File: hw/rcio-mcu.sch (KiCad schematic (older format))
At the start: 28 parts

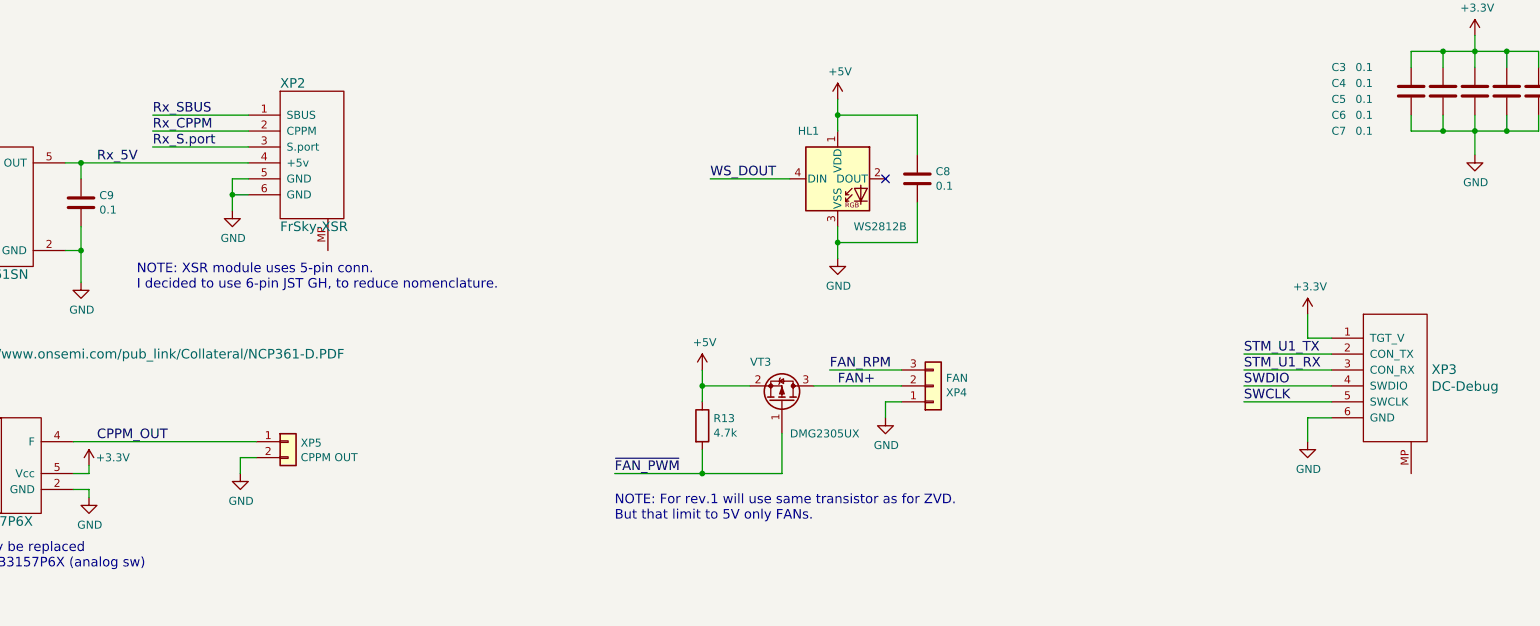
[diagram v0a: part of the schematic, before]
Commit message: hw: connect GH mount points with GND, add 3V battery
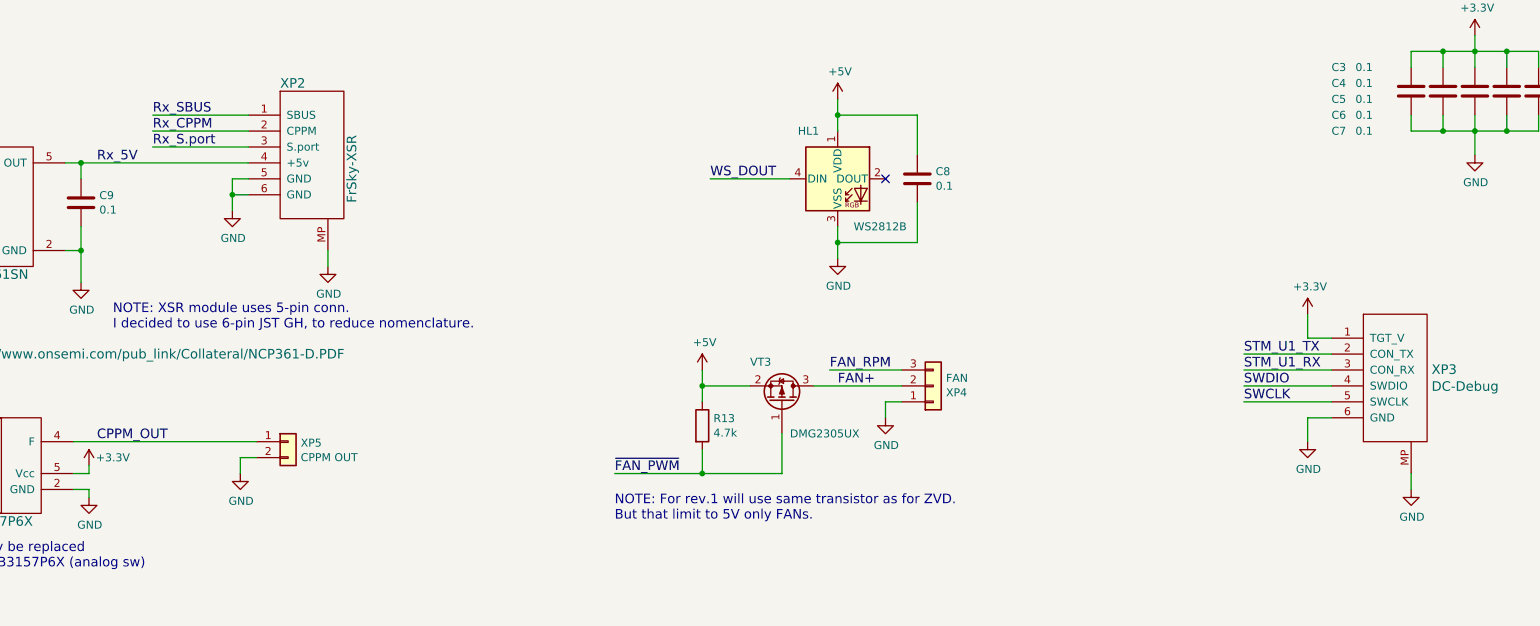
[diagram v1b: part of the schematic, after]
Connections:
- net GND: now also XP2.MP, XP3.MP
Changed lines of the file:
@@
 P 5650 6950
 F 0 "XP2" H 5450 7400 60  0000 L CNN
-F 1 "FrSky-XSR" H 5450 6500 60  0000 L CNN
+F 1 "FrSky-XSR" V 5900 6650 60  0000 L CNN
 F 2 "Connector_JST:JST_GH_SM06B-GHS-TB_1x06-1MP_P1.25mm_Horizontal" H 5650 6950 60  0001 C CNN
 F 3 "" H 5650 6950 60  0001 C CNN
@@
 	1    0    0    -1
 $EndComp
-Text Notes 4550 7800 0    60   ~ 0
+Text Notes 4400 8050 0    60   ~ 0
 NOTE: XSR module uses 5-pin conn.\nI decided to use 6-pin JST GH, to reduce nomenclature.
 $Comp
@@
 Wire Wire Line
 	10600 3250 13550 3250
+$Comp
+L power:GND #PWR?
+U 1 1 5ACFE321
+P 12550 9050
+F 0 "#PWR?" H 12550 8800 50  0001 C CNN
+F 1 "GND" H 12555 8877 50  0000 C CNN
+F 2 "" H 12550 9050 50  0001 C CNN
+F 3 "" H 12550 9050 50  0001 C CNN
+	1    12550 9050
+	1    0    0    -1
+$EndComp
+Wire Wire Line
+	12550 8950 12550 9050
+$Comp
+L power:GND #PWR?
+U 1 1 5AD073B8
+P 5750 7650
+F 0 "#PWR?" H 5750 7400 50  0001 C CNN
+F 1 "GND" H 5755 7477 50  0000 C CNN
+F 2 "" H 5750 7650 50  0001 C CNN
+F 3 "" H 5750 7650 50  0001 C CNN
+	1    5750 7650
+	1    0    0    -1
+$EndComp
+Wire Wire Line
+	5750 7650 5750 7550
 $EndSCHEMATC

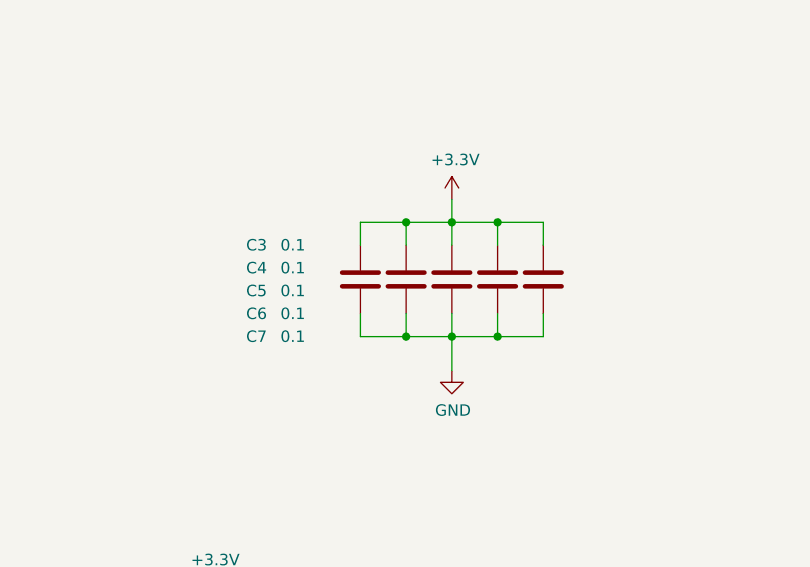
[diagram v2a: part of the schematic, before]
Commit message: hw: place all components. remove C7 0.1 coupling as not needed.
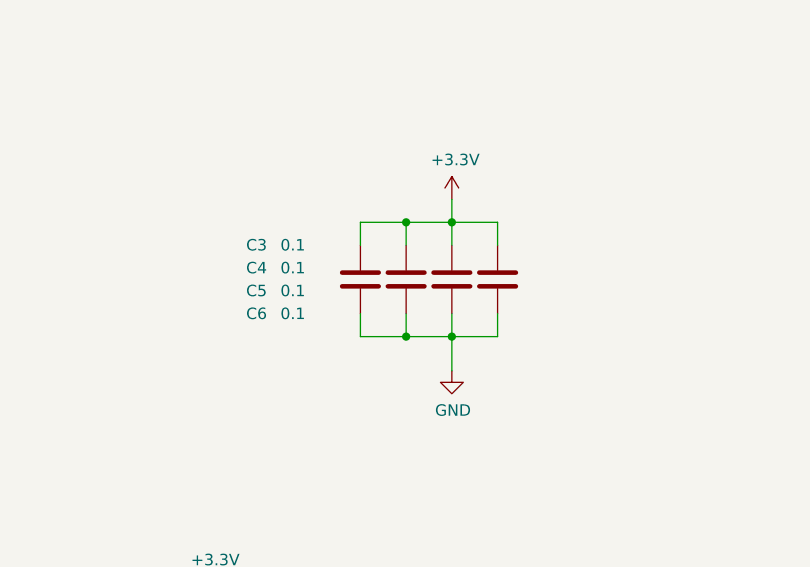
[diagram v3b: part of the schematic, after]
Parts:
- removed C7: 0.1, Capacitor_SMD:C_0603_1608Metric, symbol Device:C
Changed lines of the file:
@@
-	1    0    0    -1
-$EndComp
-$Comp
-L Device:C C7
-U 1 1 5AC31513
-P 13350 6550
-F 0 "C7" H 12050 6300 50  0000 L CNN
-F 1 "0.1" H 12200 6300 50  0000 L CNN
-F 2 "Capacitor_SMD:C_0603_1608Metric" H 13388 6400 50  0001 C CNN
-F 3 "~" H 13350 6550 50  0001 C CNN
-	1    13350 6550
 	1    0    0    -1
 $EndComp
@@
 	12550 6300 12750 6300
 Wire Wire Line
-	13350 6300 13350 6400
-Wire Wire Line
 	13150 6400 13150 6300
-Connection ~ 13150 6300
-Wire Wire Line
-	13150 6300 13350 6300
 Wire Wire Line
 	12950 6400 12950 6300
@@
 	12550 6800 12750 6800
 Wire Wire Line
-	13350 6800 13350 6700
-Wire Wire Line
 	13150 6700 13150 6800
-Connection ~ 13150 6800
-Wire Wire Line
-	13150 6800 13350 6800
 Wire Wire Line
 	12950 6700 12950 6800
